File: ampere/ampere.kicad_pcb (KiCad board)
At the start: 4 copper layers, 100 x 50 mm, 225 parts, among them J1 USB_C_Receptacle_USB2.0_16P, J2 Channel 1, J3 Channel 2, J4 Channel 3, Q10 AO4485, Q2 CSD25481F4, Q3 CSD25481F4, Q4 CSD13381F4, Q5 CSD13381F4, Q6 CSD13381F4, Q7 CSD13381F4, Q8 CSD18543Q3A, Q9 AO4485, U1 LP5907MFX-3.3, U10 TPS55289, U11 MCP4725xxx-xCH, U12 INA238, U13 INA238, U14 INA238, U15 MCP4725xxx-xCH, U18 INA238, U19 INA238, U2 STM32G474RETx, U3 TPS26750SRSMR, U4 TPD4S480RUKR, U5 CAT24C256, U6 TPS55289, U7 MIC29302WU, U8 TPS55289, U9 MIC29302WU, Y1 25 MHZ, Y2 32.768 KHZ

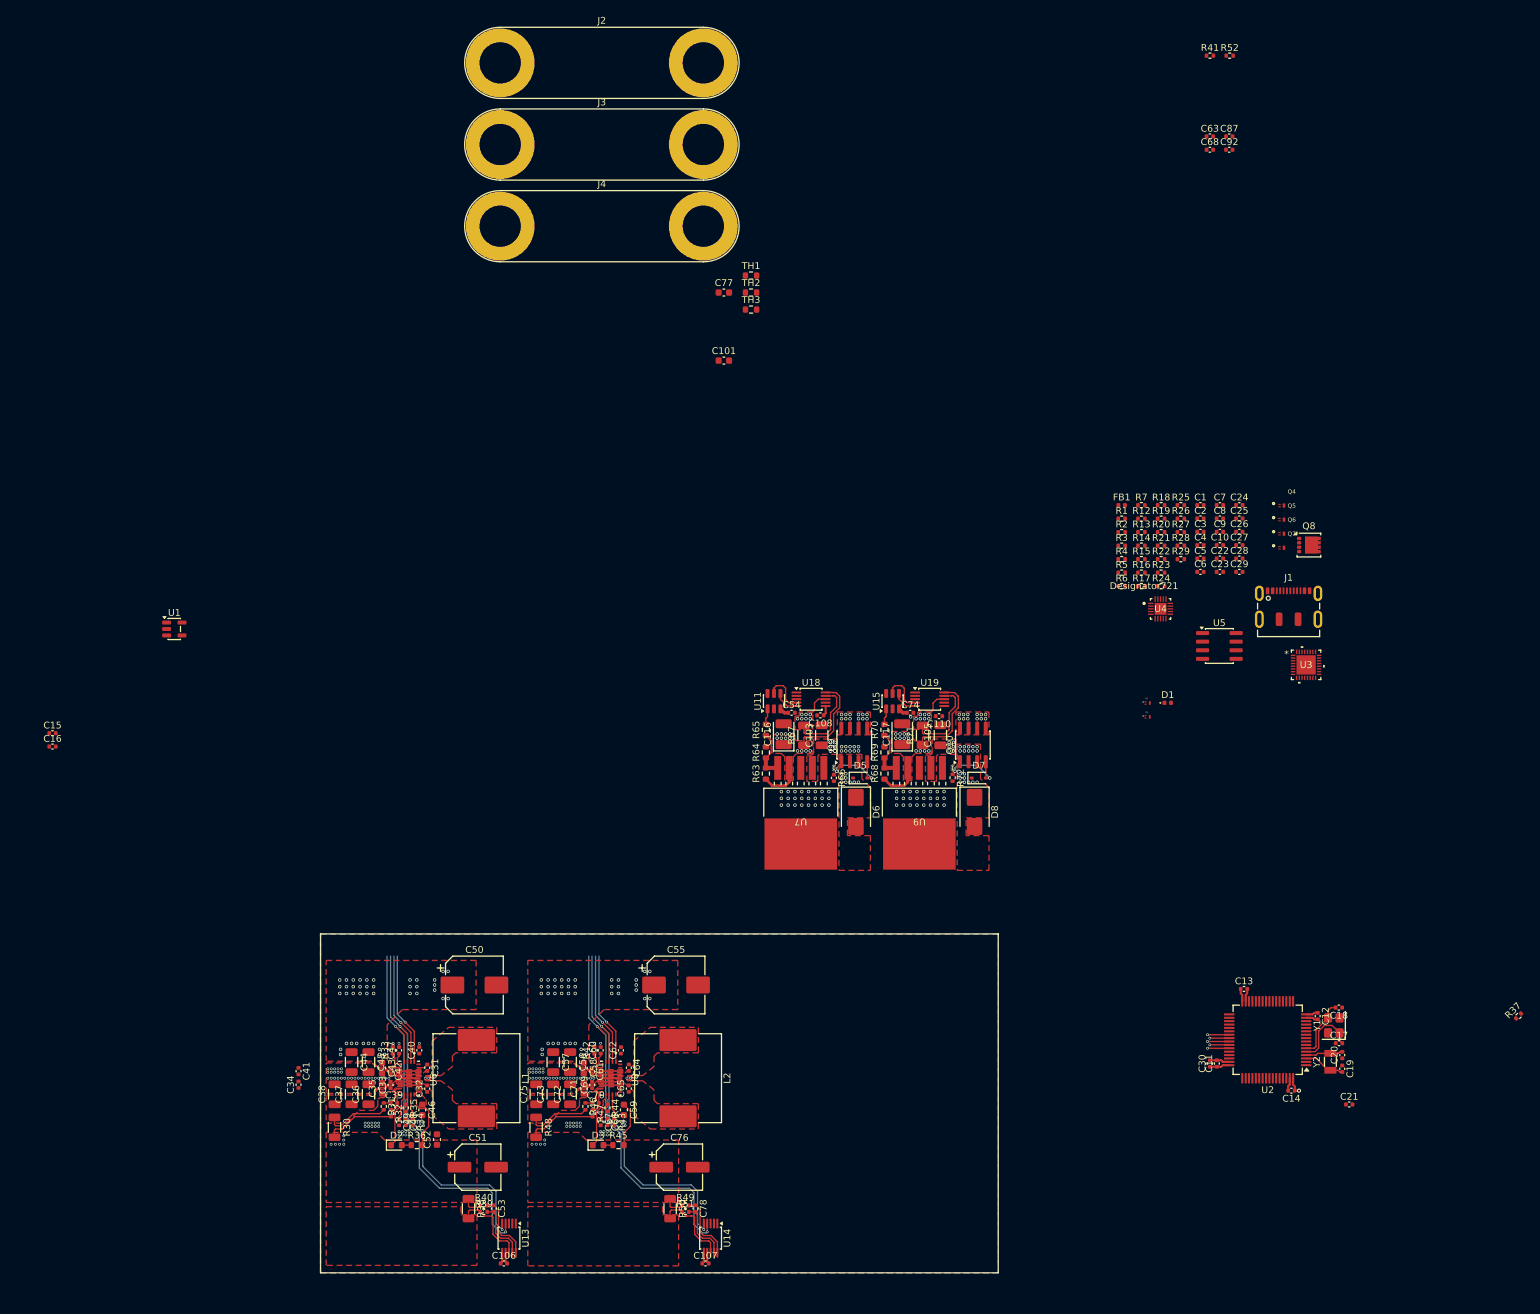
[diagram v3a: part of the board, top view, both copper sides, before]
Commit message: add lmr36520 layout, expand board size to accomedate
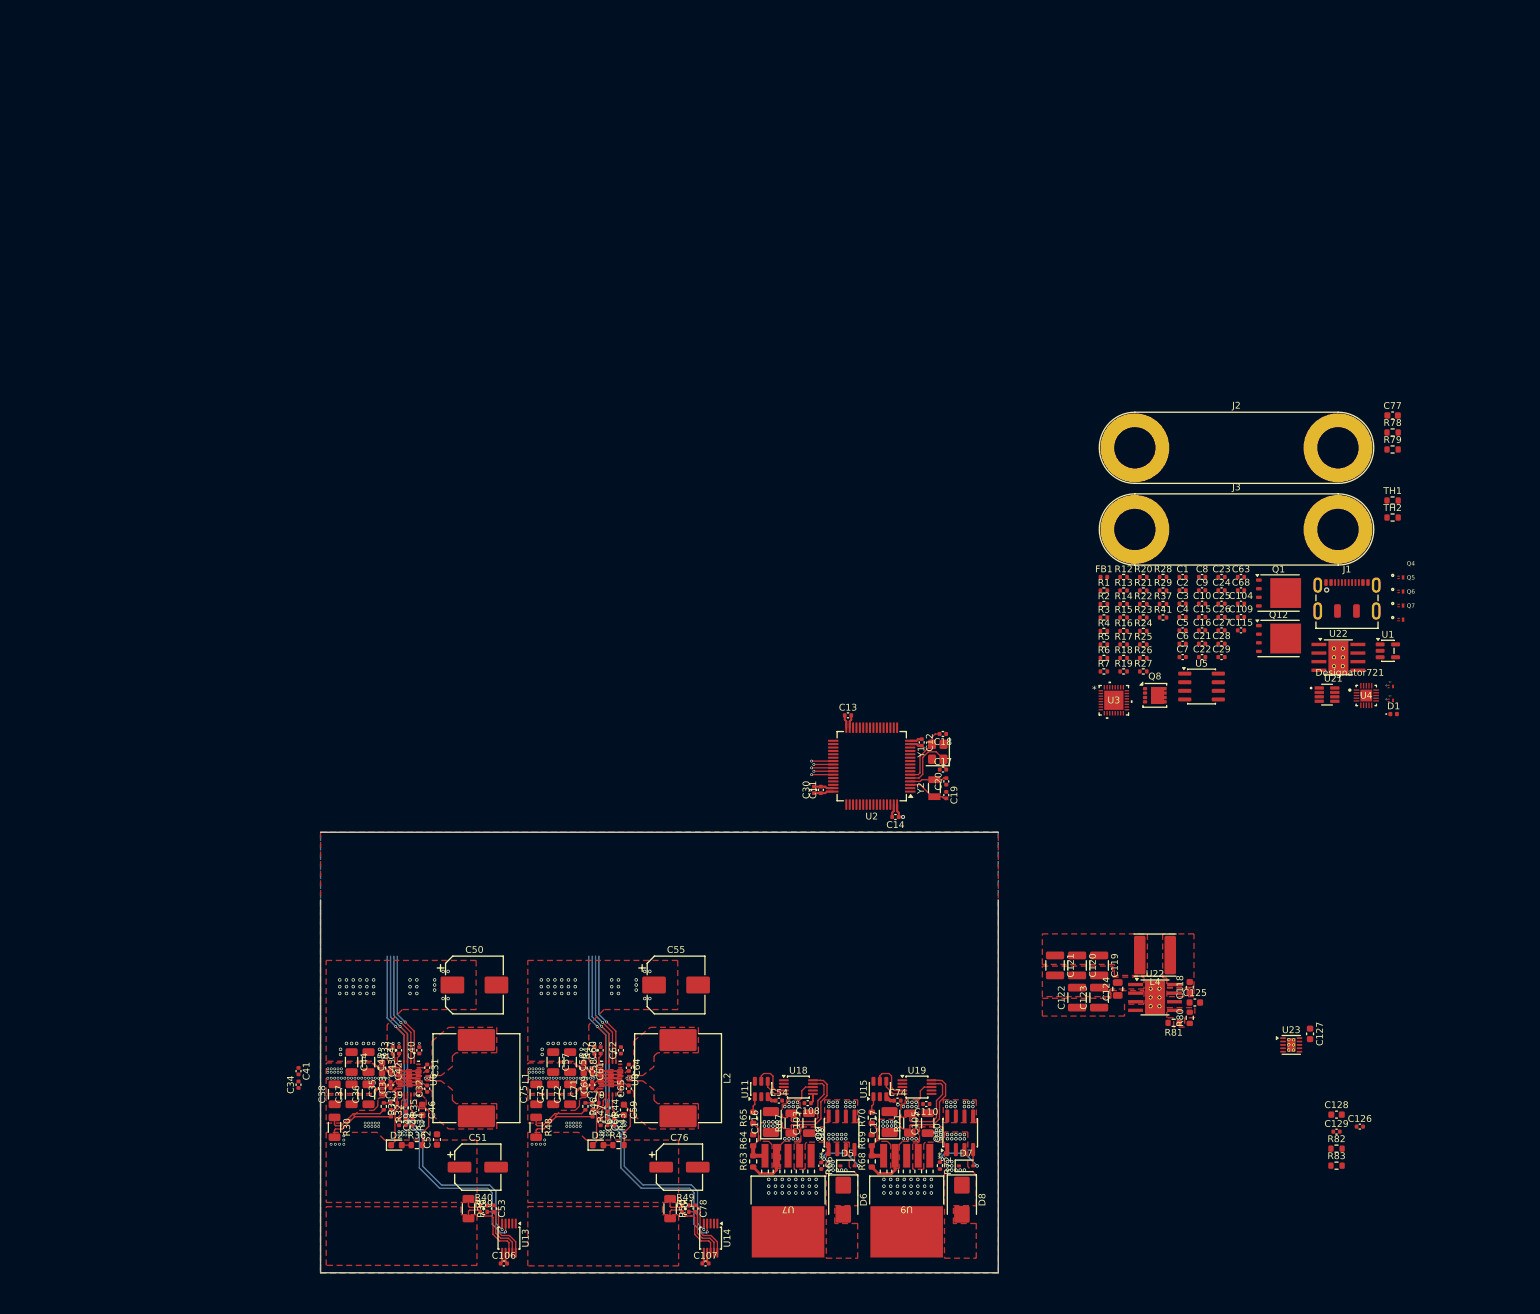
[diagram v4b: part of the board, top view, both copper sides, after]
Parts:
- removed C101: 1uF, Capacitor_SMD:C_0603_1608Metric
- removed C87, C92: 100nF, Capacitor_SMD:C_0402_1005Metric
- removed J4: Channel 3, Connector:Banana_Jack_2Pin
- removed R52: 100K, Resistor_SMD:R_0402_1005Metric
- removed TH3: Thermistor, Resistor_SMD:R_0603_1608Metric
- added C104: 220nF, Capacitor_SMD:C_0402_1005Metric, F.Cu at (221.8, 51.3)
- added C109: 220uF, Capacitor_SMD:C_0402_1005Metric, F.Cu at (221.8, 53.2)
- added C115: 10nF, Capacitor_SMD:C_0402_1005Metric, F.Cu at (221.8, 55.2)
- added C118: 100nF, Capacitor_SMD:C_0603_1608Metric, F.Cu at (214.2, 107.9)
- added C119: 22uF, Capacitor_SMD:C_1210_3225Metric, F.Cu at (200.9, 104.6)
- added C120: 22uF, Capacitor_SMD:C_1210_3225Metric, F.Cu at (197.6, 104.6)
- added C121: 22uF, Capacitor_SMD:C_1210_3225Metric, F.Cu at (194.4, 104.6)
- added C122: 4.7uF, Capacitor_SMD:C_1210_3225Metric, F.Cu at (197.6, 109.4)
- added C123: 4.7uF, Capacitor_SMD:C_1210_3225Metric, F.Cu at (200.9, 109.4)
- added C124: 220nF, Capacitor_SMD:C_0805_2012Metric, F.Cu at (203.6, 108.1)
- added C125: 1uF, Capacitor_SMD:C_0603_1608Metric, F.Cu at (215.0, 110.1)
- added C126: 10nF, Capacitor_SMD:C_0402_1005Metric, F.Cu at (239.3, 128.4)
- added C127: 10uF, Capacitor_SMD:C_0603_1608Metric, F.Cu at (232.0, 114.8)
- added C128: 10uF, Capacitor_SMD:C_0603_1608Metric, F.Cu at (235.9, 126.7)
- added C129: 100nF, Capacitor_SMD:C_0402_1005Metric, F.Cu at (235.9, 129.2)
- added L4: 12uH, Inductor_SMD:L_Changjiang_FNR6040S, F.Cu at (209.1, 103.1)
- added Q1: BSC040N08NS5, Package_TO_SOT_SMD:TDSON-8-1, F.Cu at (227.3, 49.7)
- added Q12: BSC040N08NS5, Package_TO_SOT_SMD:TDSON-8-1, F.Cu at (227.3, 56.4)
- added R78: 100K, Resistor_SMD:R_0603_1608Metric, F.Cu at (244.2, 26.0)
- added R79: 4K, Resistor_SMD:R_0603_1608Metric, F.Cu at (244.2, 28.5)
- added R80: 100K, Resistor_SMD:R_0603_1608Metric, F.Cu at (214.2, 112.4)
- added R81: 38.2K, Resistor_SMD:R_0603_1608Metric, F.Cu at (211.9, 113.1)
- added R82: 100K, Resistor_SMD:R_0603_1608Metric, F.Cu at (235.9, 131.7)
- added R83: 32.4K, Resistor_SMD:R_0603_1608Metric, F.Cu at (235.9, 134.2)
- added U21: LM74502DDFR, LM74502DDFR:SOT65P280X110-8N, F.Cu at (234.5, 64.7)
- added U22: LMR36520ADDA, Package_SO:Texas_HTSOP-8-1EP_3.9x4.9mm_P1.27mm_EP2.95x4.9mm_Mask2.4x3.1mm_ThermalVias, F.Cu at (209.1, 109.4)
- added U22: LMR36520ADDA, Package_SO:Texas_HTSOP-8-1EP_3.9x4.9mm_P1.27mm_EP2.95x4.9mm_Mask2.4x3.1mm_ThermalVias, F.Cu at (236.2, 59.2)
- added U23: TPS7A91, Package_DFN_QFN:Texas_S-PDSO-N10_EP1.2x2mm_ThermalVias, F.Cu at (229.2, 116.4)
- Q6, Q7: value CSD13381F4 -> CSD17484F4
- moved U1 179.1 mm to (243.5, 58.2)
- moved C15 170.5 mm to (216.1, 53.2)
- moved C16 170.5 mm to (216.1, 55.2)
- moved J2 109.5 mm to (206.2, 28.3)
- moved J3 109.5 mm to (206.2, 40.3)
- moved C77 100.3 mm to (244.2, 23.5)
- moved TH1 100.3 mm to (244.2, 36.1)
- moved TH2 100.3 mm to (244.2, 38.6)
- moved R41 83.2 mm to (210.3, 53.3)
- moved R37 80.3 mm to (210.3, 51.3), turned to 0 degrees
- moved C21 71.4 mm to (216.1, 57.2)
- moved C11 71.0 mm to (159.8, 78.7)
- moved C12 71.0 mm to (174.7, 71.8)
- moved C13 71.0 mm to (163.8, 67.8)
- moved C14 71.0 mm to (170.8, 82.8)
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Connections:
- C76 pad 1: Net-(C76-Pad1) -> LDO_VIN
- C77 pad 1: Net-(C76-Pad1) -> LDO_VIN
- J3 pad 1: LDO_VIN -> Net-(J3-Pin_1)
- R47 pad 2: Net-(C76-Pad1) -> LDO_VIN
- R48 pad 2: Net-(C76-Pad1) -> LDO_VIN
- R49 pad 1: Net-(C76-Pad1) -> LDO_VIN
- R50 pad 1: Net-(C76-Pad1) -> LDO_VIN
- R50 pad 2: LDO_VIN -> Net-(J3-Pin_1)
- R51 pad 1: LDO_VIN -> Net-(J3-Pin_1)
- U14 pad 8: LDO_VIN -> Net-(J3-Pin_1)
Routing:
- net Net-(C76-Pad1): track 13.2 -> 0.00 mm
- net Net-(J3-Pin_1): track 0.00 -> 12.1 mm
- net LDO_VIN: track 12.1 -> 13.2 mm
- added copper zone on F.Cu, net 3V6
- added copper zone on F.Cu, net Net-(U22-BOOT)
- added copper zone on F.Cu, net Net-(U22-FB)
- added copper zone on F.Cu, net Net-(U22-SW)
- added copper zone on F.Cu, net PPHV
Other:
- board size 100 x 50 mm -> 100 x 65 mm
